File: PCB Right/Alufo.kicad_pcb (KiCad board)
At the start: 2 copper layers, 282.6 x 90.9 mm, 93 parts, among them J2 USB_C_Receptacle_USB2.0_16P_2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, J4 USB_C_Receptacle_USB2.0_16P_2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, K11 PG1350, K12 PG1350, K13 PG1350, K14 PG1350, K15 PG1350, K16 PG1350, K21 PG1350, K22 PG1350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

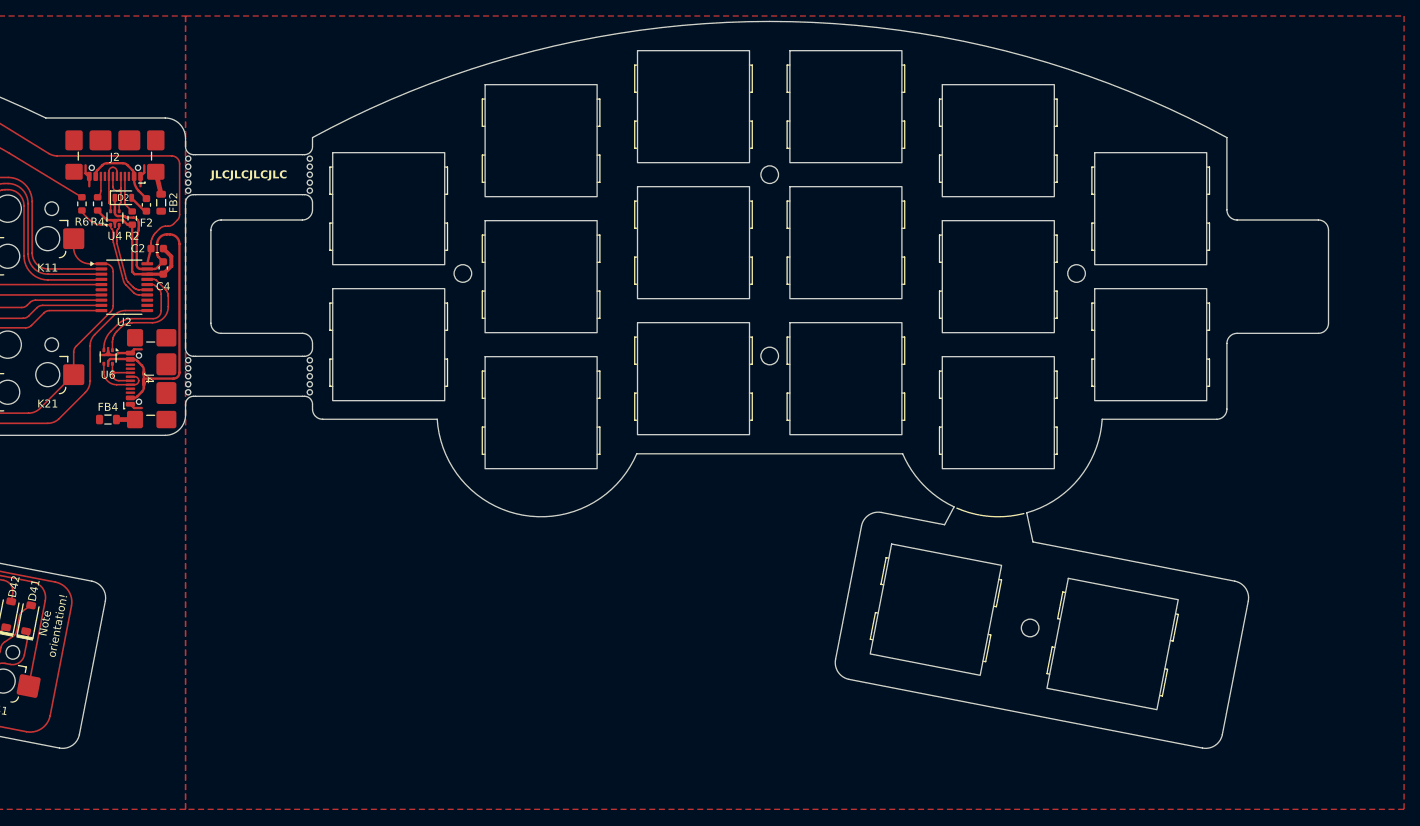
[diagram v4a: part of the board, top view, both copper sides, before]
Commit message: Fix PCB edge marker on USB port
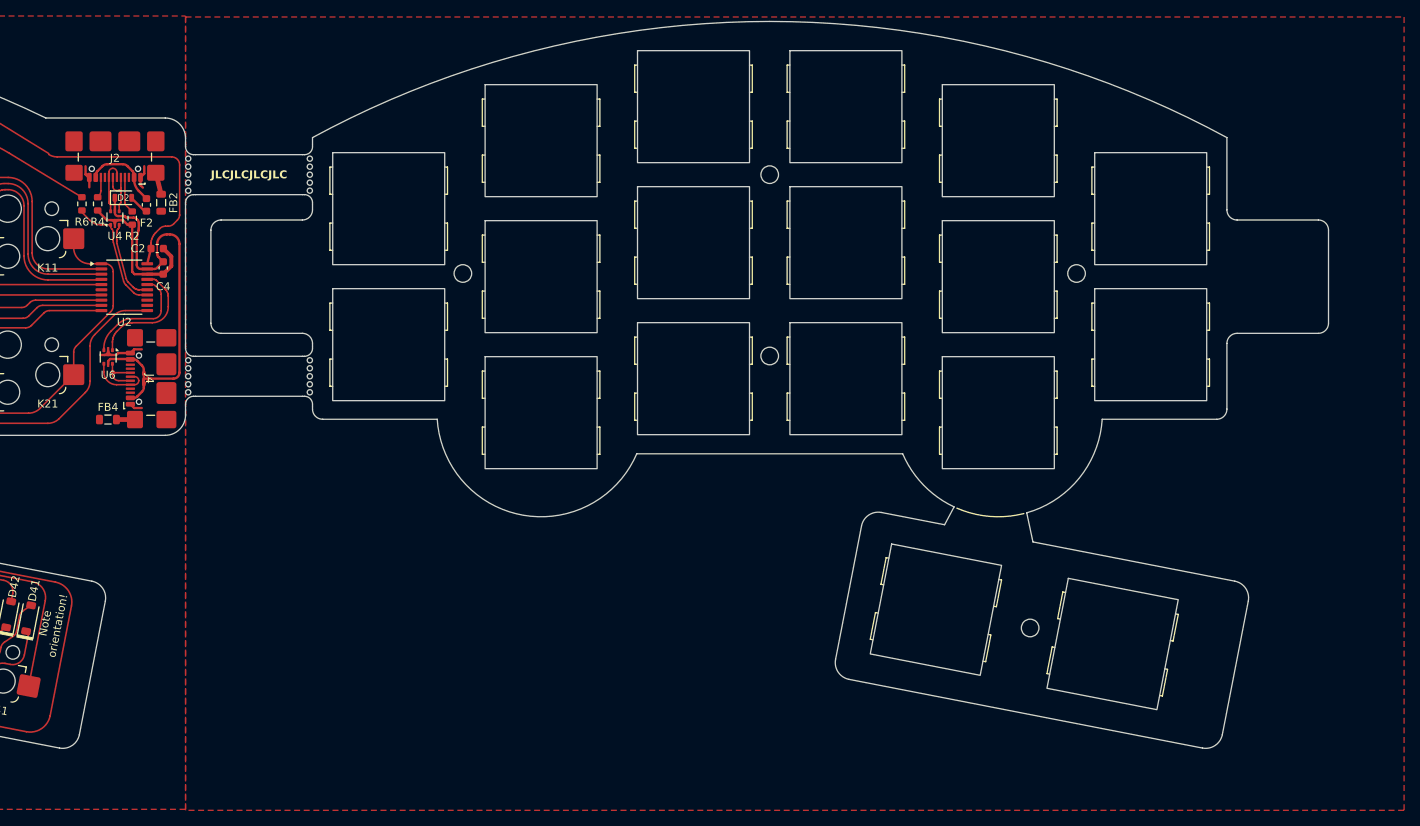
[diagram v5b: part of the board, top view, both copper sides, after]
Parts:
- moved J2 0.12 mm to (156.3, 44.8)
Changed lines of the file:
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@@
 	(footprint "Project_Library:USB_C_Receptacle_GCT_USB4110"
 		(layer "F.Cu")
-		(at 156.2705 44.704 180)
+		(at 156.2705 44.828 180)
 		(descr "USB 2.0 Type C Receptacle, GCT, 16P, top mounted, horizontal, 5A, https://gct.co/files/drawings/usb4110.pdf")
 		(tags "USB 2.0 C Type-C Receptacle SMD 16P 16C USB4110-GF-A")
@@
 		)
 		(fp_line
-			(start -5 3.675)
-			(end 5 3.675)
+			(start -5 3.745)
+			(end 5 3.745)
 			(stroke
 				(width 0.1)
@@
 		)
 		(fp_rect
-			(start -4.47 -3.675)
-			(end 4.47 3.675)
+			(start -4.47 -3.605)
+			(end 4.47 3.745)
 			(stroke
 				(width 0.1)
@@
 		)
 		(fp_line
-			(start -5 3.675)
-			(end 5 3.675)
+			(start -5 3.745)
+			(end 5 3.745)
 			(stroke
 				(width 0.1)
@@
 		)
 		(fp_rect
-			(start -4.47 -3.675)
-			(end 4.47 3.675)
+			(start -4.47 -3.605)
+			(end 4.47 3.745)
 			(stroke
 				(width 0.1)
@@
 		(pts
 			(arc
-				(start 156.7205 50.165)
-				(mid 156.932632 50.077132)
-				(end 157.0205 49.865)
+				(start 156.7205 50.155289)
+				(mid 156.932632 50.067421)
+				(end 157.0205 49.855289)
 			)
 			(arc
-				(start 157.0205 50.465)
-				(mid 156.932632 50.252868)
-				(end 156.7205 50.165)
+				(start 157.0205 50.455289)
+				(mid 156.932632 50.243157)
+				(end 156.7205 50.155289)
 			)
 		)
@@
 	)
 	(segment
-		(start 159.4705 48.384)
-		(end 159.4705 49.6155)
-		(width 0.3)
-		(layer "F.Cu")
-		(net 10)
-	)
-	(segment
 		(start 158.724 60.605)
 		(end 160.308 60.605)
@@
 	)
 	(segment
-		(start 152.9685 48.384)
-		(end 152.6015 48.017)
+		(start 152.9685 48.508)
+		(end 152.6015 48.141)
 		(width 0.3)
 		(layer "F.Cu")
@@
 	)
 	(segment
-		(start 159.4705 48.384)
-		(end 159.9395 47.915)
+		(start 159.4705 48.508)
+		(end 159.9395 48.039)
 		(width 0.3)
 		(layer "F.Cu")
@@
 	)
 	(segment
-		(start 152.6015 48.017)
-		(end 152.6015 46.99)
+		(start 159.4705 49.4885)
+		(end 159.766 49.784)
+		(width 0.3)
+		(layer "F.Cu")
+		(net 10)
+	)
+	(segment
+		(start 152.6015 48.141)
+		(end 152.6015 47.114)
+		(width 0.3)
+		(layer "F.Cu")
+		(net 10)
+	)
+	(segment
+		(start 159.4705 48.508)
+		(end 159.4705 49.4885)
 		(width 0.3)
 		(layer "F.Cu")
@@
 	)
 	(segment
-		(start 153.0705 48.384)
-		(end 153.0705 49.6215)
+		(start 153.0705 48.508)
+		(end 153.0705 49.7455)
 		(width 0.3)
 		(layer "F.Cu")
@@
 	)
 	(segment
-		(start 159.9395 47.915)
-		(end 159.9395 46.99)
+		(start 159.9395 48.039)
+		(end 159.9395 47.114)
 		(width 0.3)
 		(layer "F.Cu")
@@
 	)
 	(segment
-		(start 163.359 45.8216)
-		(end 149.054753 45.8216)
+		(start 163.359 45.9456)
+		(end 149.054753 45.9456)
 		(width 0.2)
 		(layer "F.Cu")
@@
 	)
 	(segment
-		(start 164.359 53.158786)
-		(end 164.359 46.8216)
+		(start 164.359 53.282786)
+		(end 164.359 46.9456)
 		(width 0.2)
 		(layer "F.Cu")
@@
 	)
 	(arc
-		(start 148.006135 45.524656)
-		(mid 148.509827 45.745933)
-		(end 149.054753 45.8216)
+		(start 148.006135 45.648656)
+		(mid 148.509827 45.869933)
+		(end 149.054753 45.9456)
 		(width 0.2)
 		(layer "F.Cu")
@@
 	)
 	(arc
-		(start 164.359 46.8216)
-		(mid 164.066107 46.114493)
-		(end 163.359 45.8216)
+		(start 164.359 46.9456)
+		(mid 164.066107 46.238493)
+		(end 163.359 45.9456)
 		(width 0.2)
 		(layer "F.Cu")
@@
 	)
 	(segment
-		(start 161.3805 47.809)
+		(start 161.3805 47.933)
 		(end 162.052 50.6105)
 		(width 0.6)
@@
 	)
 	(segment
-		(start 157.5205 48.749)
+		(start 157.5205 48.508)
 		(end 157.5205 51.649893)
 		(width 0.2)
@@
 	)
 	(segment
-		(start 154.5205 48.384)
-		(end 154.5205 50.170786)
+		(start 154.5205 50.170786)
+		(end 154.5205 48.508)
 		(width 0.2)
 		(layer "F.Cu")
@@
 	)
 	(segment
-		(start 157.835315 46.970315)
-		(end 158.486186 47.621186)
+		(start 157.835315 47.094315)
+		(end 158.486186 47.745186)
 		(width 0.3)
 		(layer "F.Cu")
@@
 	)
 	(segment
-		(start 154.054815 47.639685)
-		(end 154.724186 46.970314)
+		(start 159.256287 50.201287)
+		(end 160.2105 51.1555)
 		(width 0.3)
 		(layer "F.Cu")
@@
 	)
 	(segment
-		(start 155.289871 46.736)
-		(end 157.269629 46.736)
+		(start 154.054815 47.763685)
+		(end 154.724186 47.094314)
 		(width 0.3)
 		(layer "F.Cu")
@@
 	)
 	(segment
-		(start 159.256287 50.201287)
-		(end 160.2105 51.1555)
+		(start 155.289871 46.86)
+		(end 157.269629 46.86)
 		(width 0.3)
 		(layer "F.Cu")
@@
 	)
 	(arc
-		(start 158.7205 48.186871)
-		(mid 158.659604 47.880725)
-		(end 158.486186 47.621186)
+		(start 159.256287 50.201287)
+		(mid 158.822741 49.55244)
+		(end 158.6705 48.787073)
 		(width 0.3)
 		(layer "F.Cu")
@@
 	)
 	(arc
-		(start 157.269629 46.736)
-		(mid 157.575776 46.796897)
-		(end 157.835315 46.970315)
+		(start 158.7205 48.310871)
+		(mid 158.659604 48.004725)
+		(end 158.486186 47.745186)
 		(width 0.3)
 		(layer "F.Cu")
@@
 	)
 	(arc
-		(start 153.8205 48.205371)
-		(mid 153.881397 47.899224)
-		(end 154.054815 47.639685)
+		(start 157.269629 46.86)
+		(mid 157.575776 46.920897)
+		(end 157.835315 47.094315)
 		(width 0.3)
 		(layer "F.Cu")
@@
 	)
 	(arc
-		(start 159.256287 50.201287)
-		(mid 158.822741 49.55244)
-		(end 158.6705 48.787073)
+		(start 153.8205 48.329371)
+		(mid 153.881397 48.023224)
+		(end 154.054815 47.763685)
 		(width 0.3)
 		(layer "F.Cu")
@@
 	)
 	(arc
-		(start 155.289871 46.736)
-		(mid 154.983725 46.796896)
-		(end 154.724186 46.970314)
+		(start 155.289871 46.86)
+		(mid 154.983725 46.920896)
+		(end 154.724186 47.094314)
 		(width 0.3)
 		(layer "F.Cu")
@@
 	)
 	(segment
-		(start 155.561505 51.745005)
-		(end 155.688995 51.872495)
+		(start 155.5205 51.64601)
+		(end 155.5205 48.508)
 		(width 0.2)
 		(layer "F.Cu")
@@
 	)
 	(segment
-		(start 155.5205 48.749)
-		(end 155.5205 47.749)
+		(start 155.561505 51.745005)
+		(end 155.688995 51.872495)
 		(width 0.2)
 		(layer "F.Cu")
@@
 	)
 	(segment
-		(start 155.73 51.97149)
-		(end 155.73 52.744)
+		(start 156.5205 48.508)
+		(end 156.5205 47.873)
 		(width 0.2)
 		(layer "F.Cu")
@@
 	)
 	(segment
-		(start 156.5205 48.749)
-		(end 156.5205 47.749)
+		(start 155.5205 48.508)
+		(end 155.5205 47.873)
 		(width 0.2)
 		(layer "F.Cu")
@@
 	)
 	(segment
-		(start 155.5205 48.749)
-		(end 155.5205 51.64601)
+		(start 155.73 51.97149)
+		(end 155.73 52.744)
 		(width 0.2)
 		(layer "F.Cu")
@@
 	)
 	(arc
-		(start 155.5205 47.749)
-		(mid 155.666947 47.395447)
-		(end 156.0205 47.249)
+		(start 155.5205 47.873)
+		(mid 155.666947 47.519447)
+		(end 156.0205 47.373)
 		(width 0.2)
 		(layer "F.Cu")
@@
 	)
 	(arc
-		(start 156.5205 47.749)
-		(mid 156.374053 47.395447)
-		(end 156.0205 47.249)
+		(start 156.5205 47.873)
+		(mid 156.374053 47.519447)
+		(end 156.0205 47.373)
 		(width 0.2)
 		(layer "F.Cu")
@@
 	)
 	(segment
-		(start 157.0205 48.384)
-		(end 157.0205 49.865)
-		(width 0.2)
-		(layer "F.Cu")
-		(net 68)
-	)
-	(segment
 		(start 156.805 51.96249)
 		(end 156.805 52.744)
@@
 	)
 	(segment
-		(start 156.447899 50.165)
-		(end 156.7205 50.165)
+		(start 156.5205 50.155289)
+		(end 156.7205 50.155289)
 		(width 0.2)
 		(layer "F.Cu")
@@
 	)
 	(segment
-		(start 156.979495 51.730005)
-		(end 156.846005 51.863495)
+		(start 157.017618 50.0481)
+		(end 157.0205 48.508)
 		(width 0.2)
 		(layer "F.Cu")
@@
 	)
 	(segment
-		(start 156.0135 49.666711)
-		(end 156.0205 49.659711)
+		(start 156.0205 48.508)
+		(end 156.0205 49.655289)
 		(width 0.2)
 		(layer "F.Cu")
@@
 	)
 	(segment
-		(start 156.0205 49.659711)
-		(end 156.0205 48.384)
+		(start 156.979495 51.730005)
+		(end 156.846005 51.863495)
 		(width 0.2)
 		(layer "F.Cu")
@@
 	)
 	(arc
-		(start 156.0135 49.666711)
-		(mid 156.13758 49.996384)
-		(end 156.447899 50.165)
+		(start 156.805 51.96249)
+		(mid 156.815657 51.908914)
+		(end 156.846005 51.863495)
 		(width 0.2)
 		(layer "F.Cu")
@@
 	)
 	(arc
-		(start 156.805 51.96249)
-		(mid 156.815657 51.908914)
-		(end 156.846005 51.863495)
+		(start 156.0205 49.655289)
+		(mid 156.166947 50.008842)
+		(end 156.5205 50.155289)
 		(width 0.2)
 		(layer "F.Cu")
@@
 		(polygon
 			(pts
-				(xy 165.1 28.33334) (xy 317.417601 28.33334) (xy 317.417601 127.50003) (xy 165.1 127.50003)
+				(xy 165.1 28.45734) (xy 317.417601 28.45734) (xy 317.417601 127.62403) (xy 165.1 127.62403)
 			)
 		)

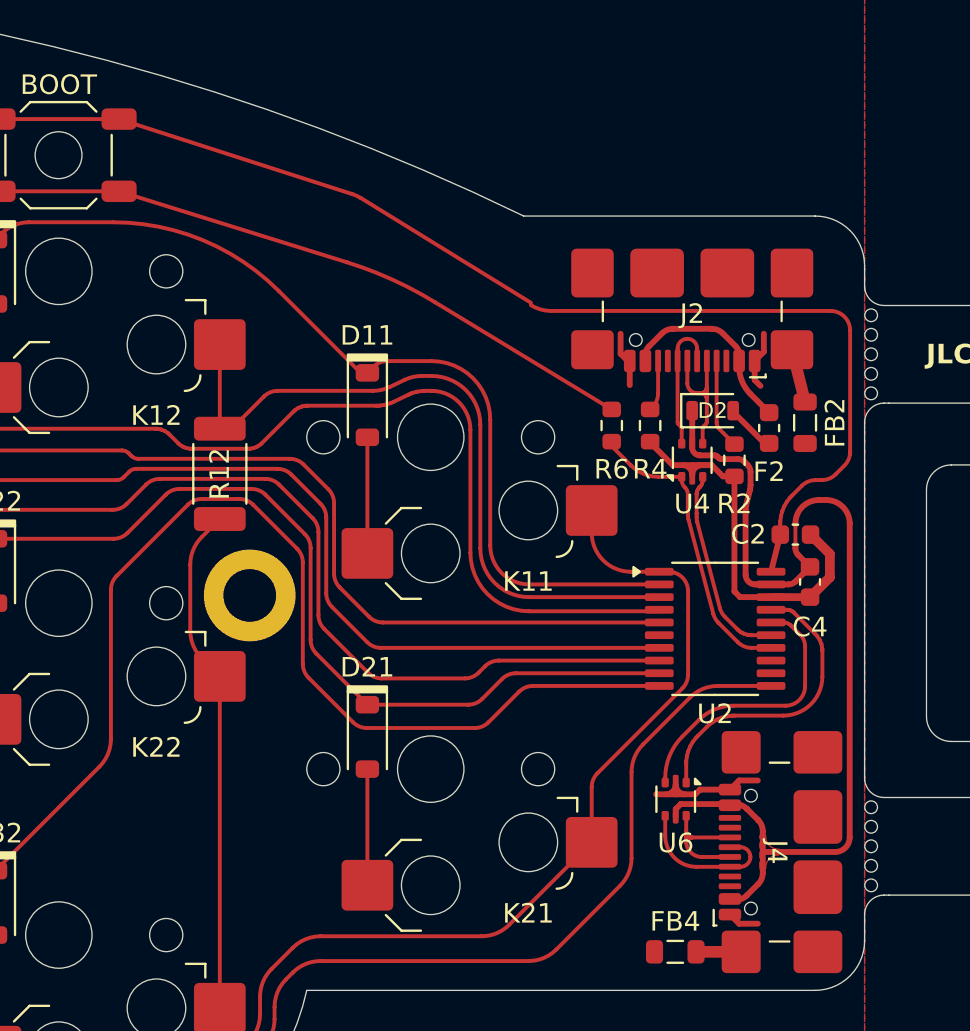
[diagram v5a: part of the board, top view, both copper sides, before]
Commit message: Update extra USB port solder pad
The pad should now not overlap with parts of the port casing that have no metal.
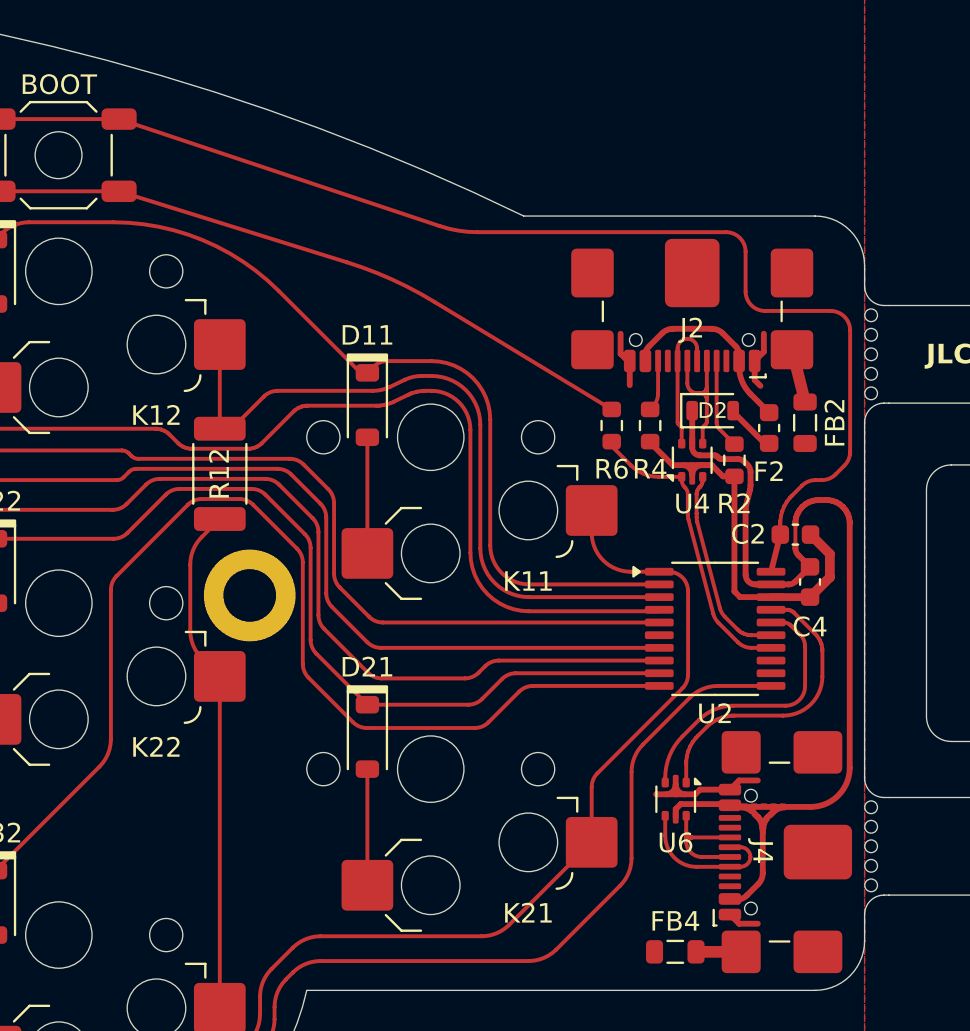
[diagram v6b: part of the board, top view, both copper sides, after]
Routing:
- net +3V3: track 86.3 -> 88.1 mm

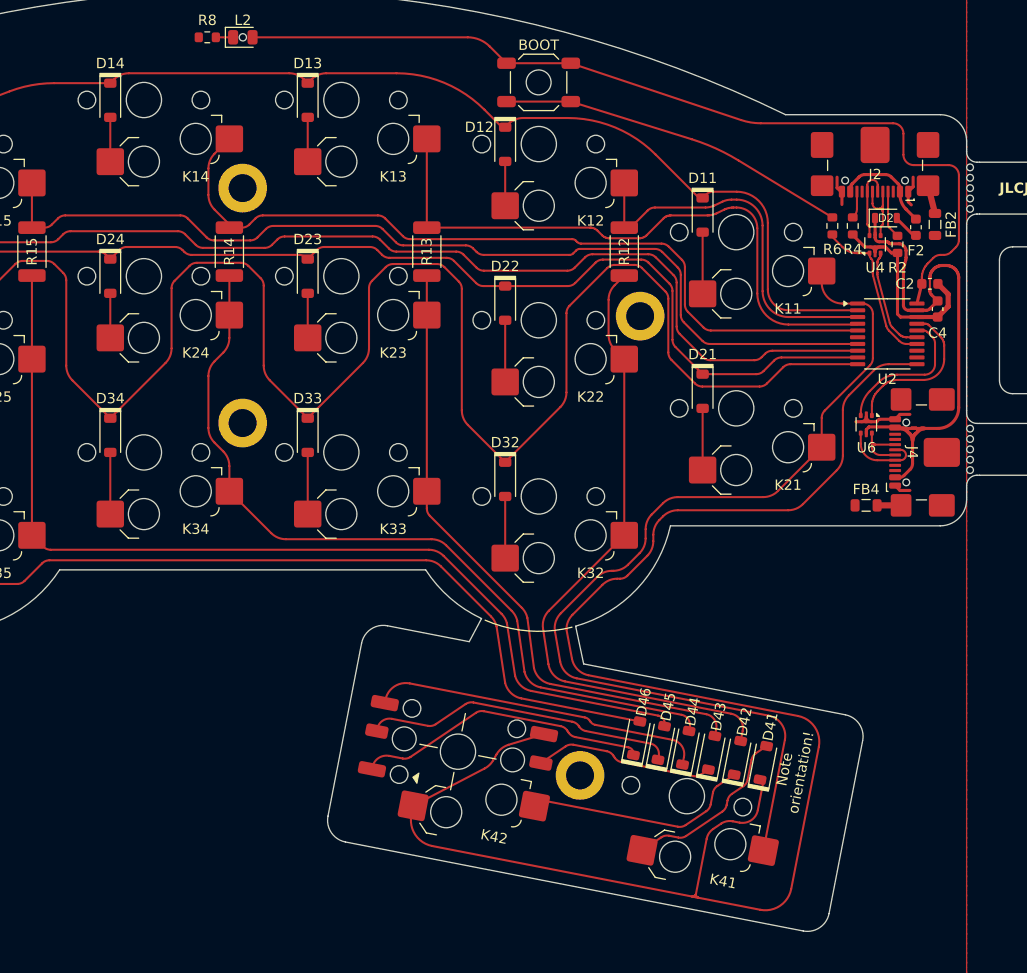
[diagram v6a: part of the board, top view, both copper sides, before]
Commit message: Relocate righthand MCU
Routing and layout is a bit better now.
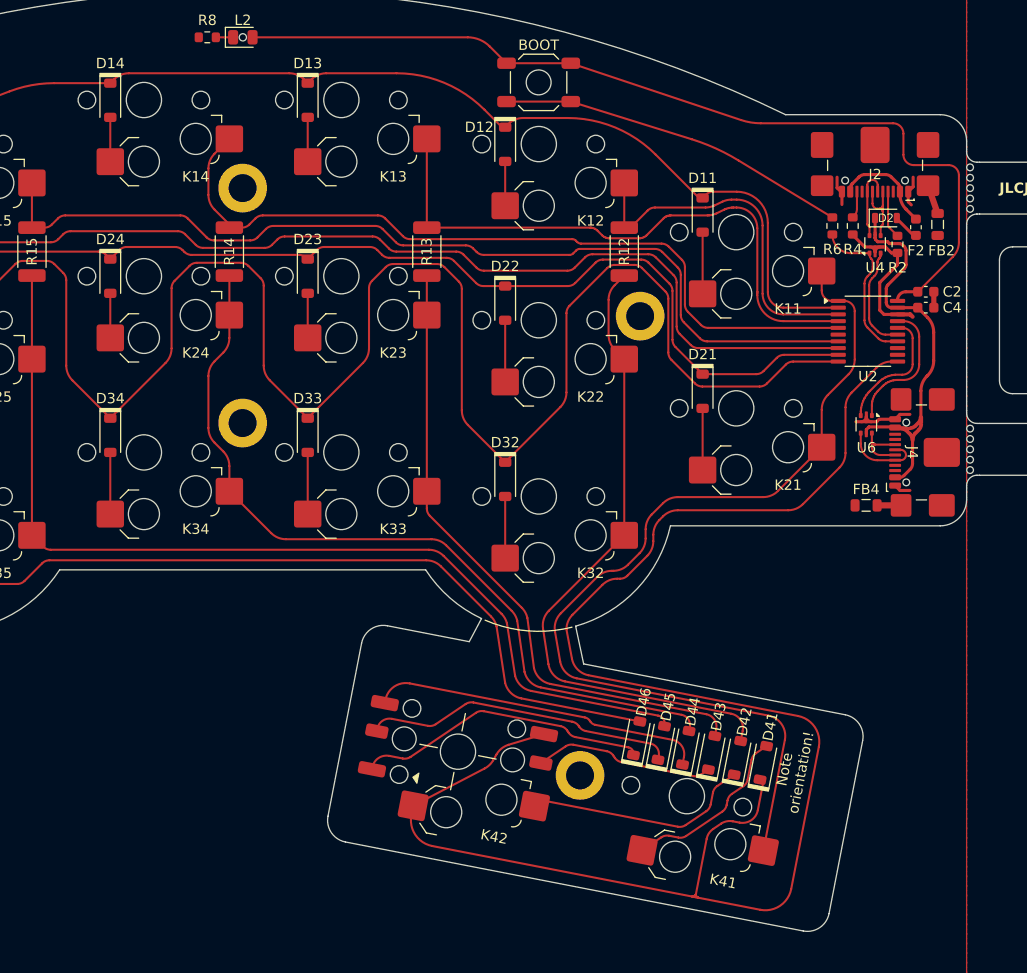
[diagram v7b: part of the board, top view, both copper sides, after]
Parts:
- moved U2 1.89 mm to (155.6, 62.0)
- moved C4 1.15 mm to (161.2, 59.7), turned to 0 degrees
- moved C2 0.86 mm to (161.2, 58.2)
- moved FB2 0.25 mm to (162.3, 51.7)
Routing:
- net VCC: track 51.8 -> 40.0 mm
- net RX: track 15.4 -> 12.6 mm
- net Col6: track 230.0 -> 227.4 mm
- net GND: track 28.5 -> 25.9 mm
- net TX: track 14.4 -> 11.9 mm
- net Row4: track 162.0 -> 159.6 mm
- net Col5: track 92.1 -> 90.1 mm
- net Col4: track 76.4 -> 74.4 mm
- net Row1: track 119.6 -> 117.7 mm
- net Col2: track 35.7 -> 33.8 mm
- net Col3: track 60.4 -> 58.6 mm
- net Row2: track 121.7 -> 119.9 mm
- net Row3: track 184.7 -> 183.0 mm
- net Col1: track 93.6 -> 91.9 mm
- net +3V3: track 88.1 -> 88.8 mm
